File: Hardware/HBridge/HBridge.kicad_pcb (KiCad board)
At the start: 2 copper layers, 55.8 x 33.6 mm, 36 parts, among them IC1 SP8M4HZGTB, IC2 SP8M4HZGTB, J1 Conn_01x03_Pin, J2 Conn_01x04_Pin, U1 TC4427xOA, U2 TC4427xOA

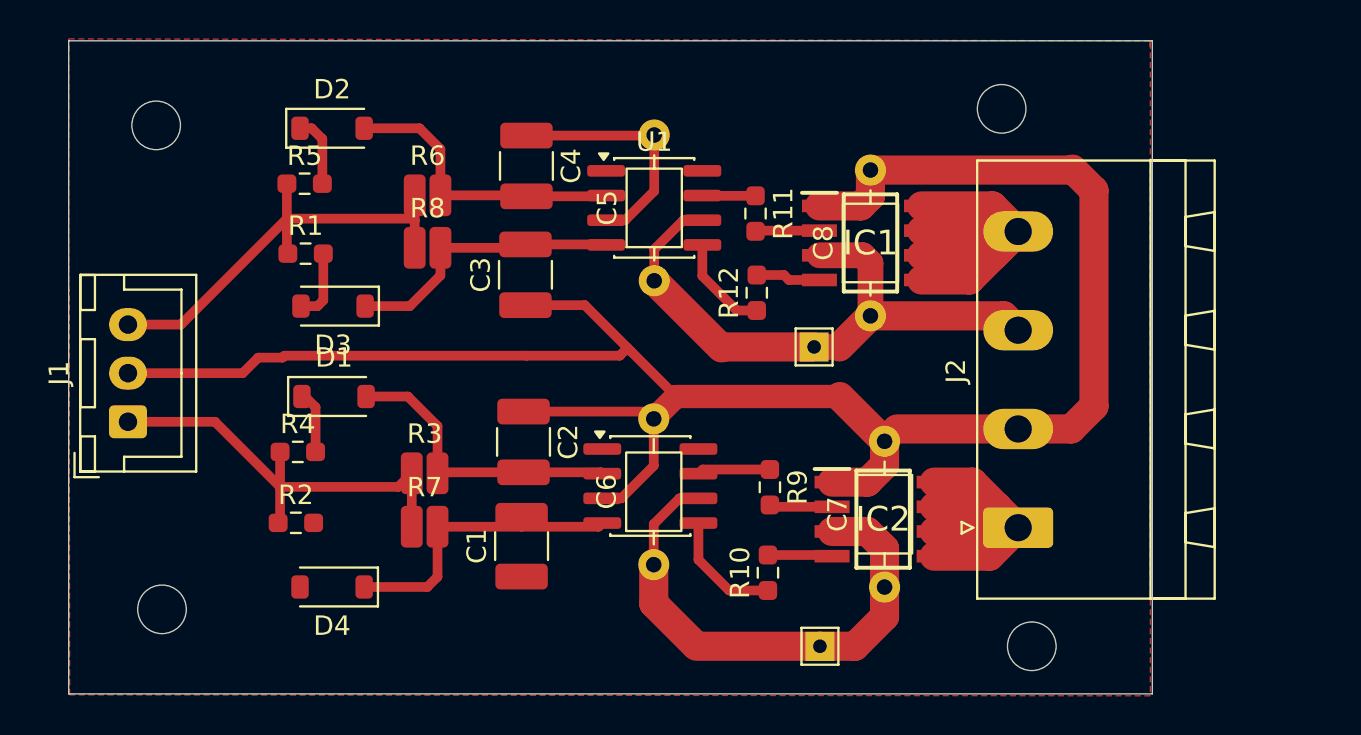
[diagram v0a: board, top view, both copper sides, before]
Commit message: Add Schottky diode component to HBridge schematic
- Introduced a new Schottky diode symbol with reference designators D5 and D6.
- Updated properties including Value, Footprint, and Description for the new diode.
- Added necessary junctions and wires to integrate the diode into the existing circuit.
- Ensured the new component is included in the BOM and is visible on the board.
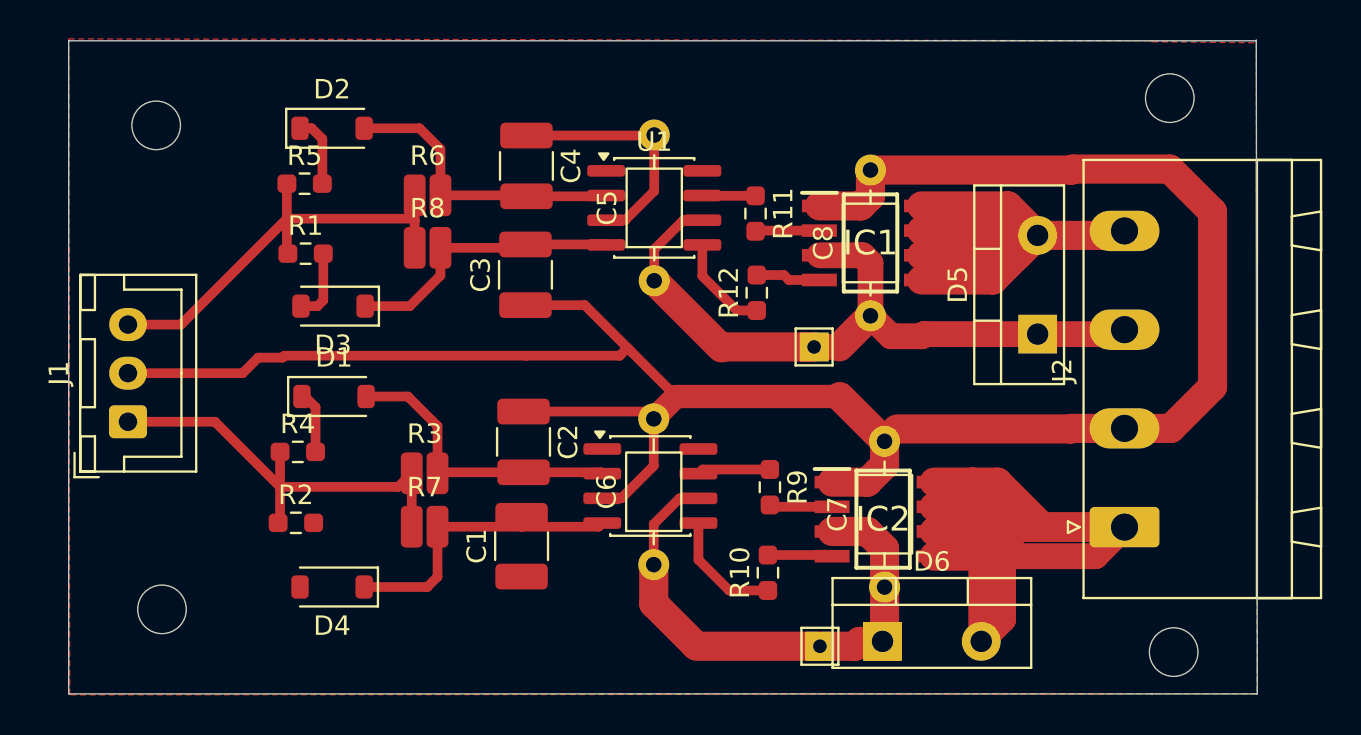
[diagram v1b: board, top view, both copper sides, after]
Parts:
- added D5: D_Schottky, Package_TO_SOT_THT:TO-220-2_Vertical, F.Cu at (145.1, 67.2)
- added D6: D_Schottky, Package_TO_SOT_THT:TO-220-2_Vertical, F.Cu at (137.1, 83.0)
- moved REF** 8.67 mm to (151.9, 55.0)
- moved REF** 7.31 mm to (152.1, 83.5)
- moved J2 5.47 mm to (149.6, 77.1)
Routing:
- net O2: track 19.4 -> 50.5 mm
- net MGND: track 117.5 -> 128.5 mm
- net O1: track 22.0 -> 30.6 mm
- net Vm: track 58.3 -> 64.8 mm
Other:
- board size 55.8 x 33.6 mm -> 61.2 x 33.7 mm
